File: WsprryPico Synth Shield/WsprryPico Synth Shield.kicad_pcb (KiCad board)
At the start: 2 copper layers, 53.3 x 22.9 mm, 1 part

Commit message: Set up schematic
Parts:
- U11: moved to B.Cu
- moved U11 1.95 mm to (146.8, 90.8), turned to -90 degrees
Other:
- outline, holes or cut-outs redrawn

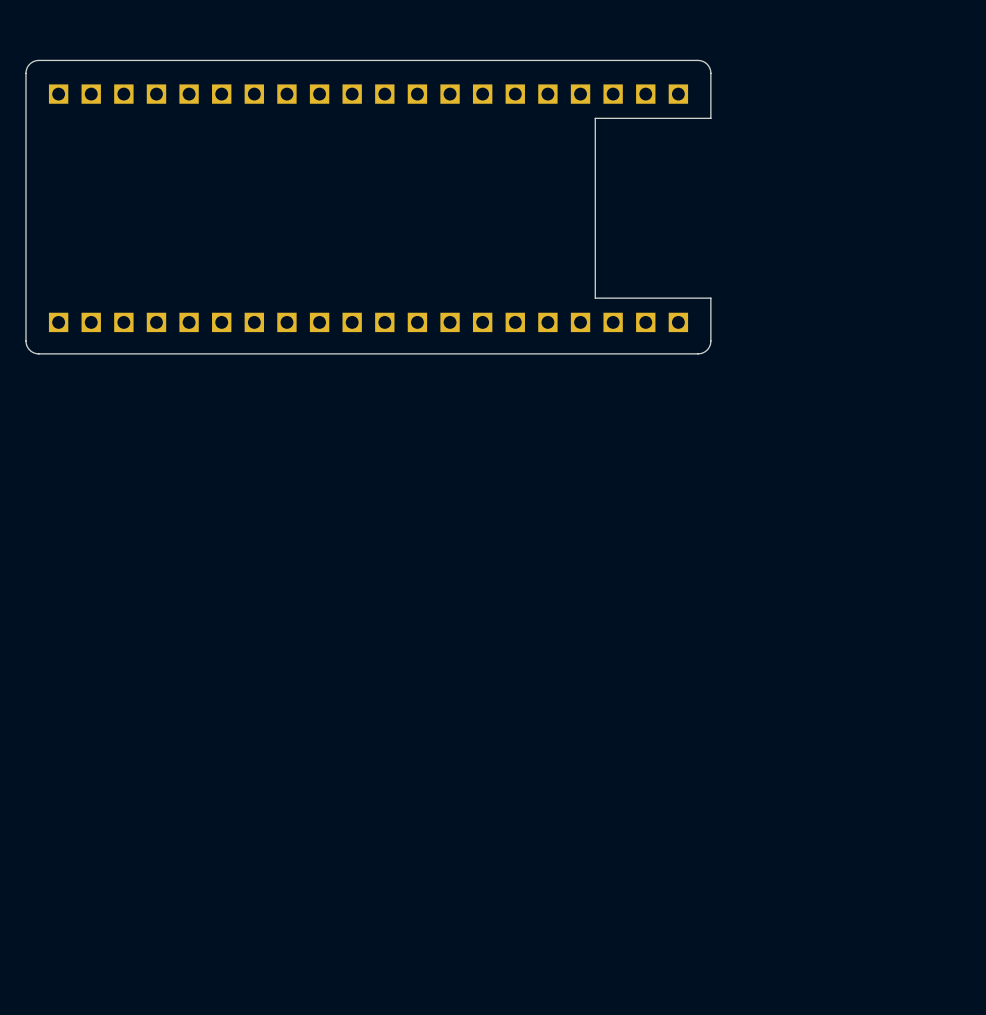
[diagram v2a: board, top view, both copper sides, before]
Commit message: Add single-post QLG3 variant and restore edge-launch SMA
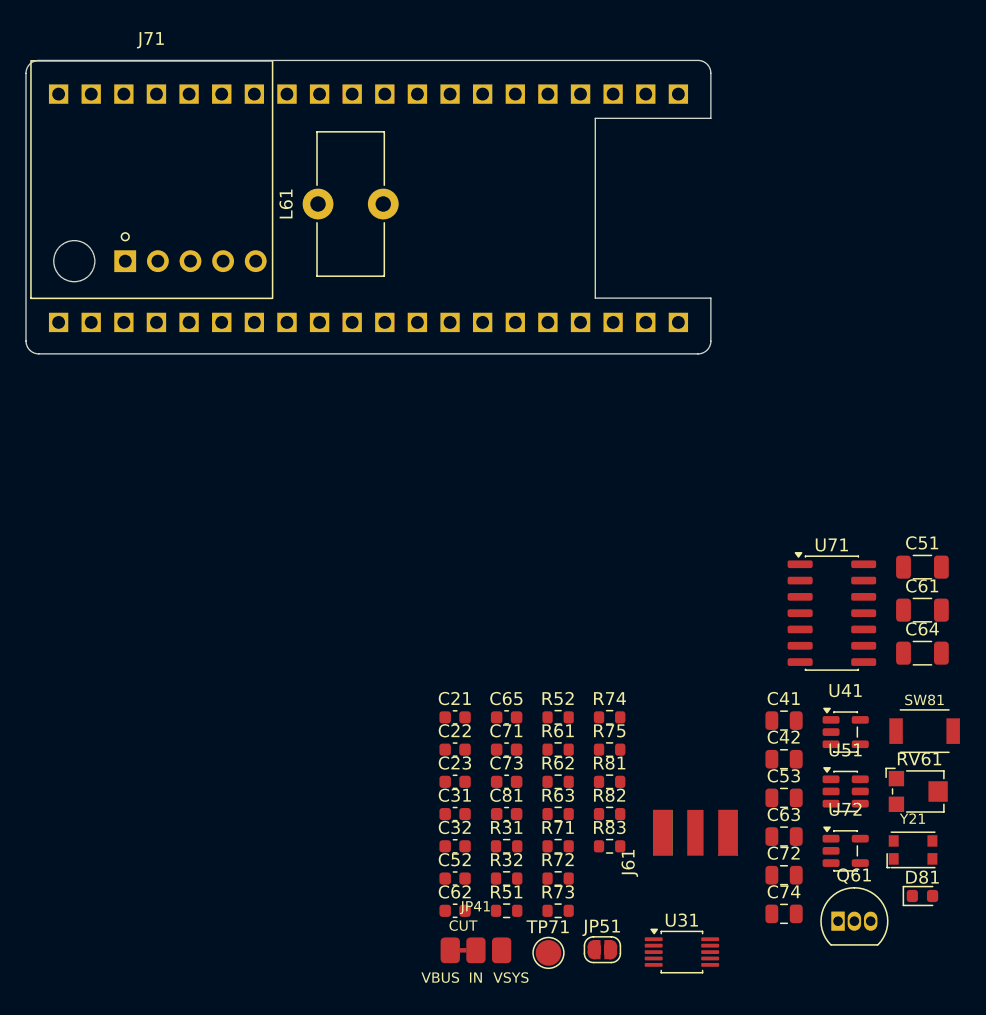
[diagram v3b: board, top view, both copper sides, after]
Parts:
- added C21: 10nF, wsprrypico-synth-shield:C_0603_1608Metric, F.Cu at (153.5, 129.5)
- added C22: 1nF C0G, wsprrypico-synth-shield:C_0603_1608Metric, F.Cu at (153.5, 132.0)
- added C23: 100nF, wsprrypico-synth-shield:C_0603_1608Metric, F.Cu at (153.5, 134.5)
- added C31: 100nF, wsprrypico-synth-shield:C_0603_1608Metric, F.Cu at (153.5, 137.0)
- added C32: 100nF, wsprrypico-synth-shield:C_0603_1608Metric, F.Cu at (153.5, 139.5)
- added C41: 2.2μF, wsprrypico-synth-shield:C_0805_2012Metric, F.Cu at (179.2, 129.8)
- added C42: 2.2μF, wsprrypico-synth-shield:C_0805_2012Metric, F.Cu at (179.2, 132.8)
- added C51: 10μF, wsprrypico-synth-shield:C_1206_3216Metric, F.Cu at (189.9, 117.8)
- added C52: 1nF, wsprrypico-synth-shield:C_0603_1608Metric, F.Cu at (153.5, 142.1)
- added C53: 1μF, wsprrypico-synth-shield:C_0805_2012Metric, F.Cu at (179.2, 135.8)
- added C61: 100nF, wsprrypico-synth-shield:C_1206_3216Metric, F.Cu at (189.9, 121.2)
- added C62: 100nF, wsprrypico-synth-shield:C_0603_1608Metric, F.Cu at (153.5, 144.6)
- added C63: 1μF, wsprrypico-synth-shield:C_0805_2012Metric, F.Cu at (179.2, 138.8)
- added C64: 100nF, wsprrypico-synth-shield:C_1206_3216Metric, F.Cu at (189.9, 124.5)
- added C65: 100nF, wsprrypico-synth-shield:C_0603_1608Metric, F.Cu at (157.6, 129.5)
- added C71: 100nF, wsprrypico-synth-shield:C_0603_1608Metric, F.Cu at (157.6, 132.0)
- added C72: 1μF, wsprrypico-synth-shield:C_0805_2012Metric, F.Cu at (179.2, 141.8)
- added C73: 100nF, wsprrypico-synth-shield:C_0603_1608Metric, F.Cu at (157.6, 134.5)
- added C74: 2.2μF, wsprrypico-synth-shield:C_0805_2012Metric, F.Cu at (179.2, 144.8)
- added C81: 10nF, wsprrypico-synth-shield:C_0603_1608Metric, F.Cu at (157.6, 137.0)
- added D81: Red, wsprrypico-synth-shield:LED_0603_1608Metric, F.Cu at (189.9, 143.4)
- added J61: SMA 50ohm, wsprrypico-synth-shield:SMA_Adafruit_1865_EdgeMount, F.Cu at (172.3, 140.8)
- added J71: QLG3 GPS Receiver, wsprrypico-synth-shield:QLG3_GPS_UndersideHeader_SinglePost, F.Cu at (120.7, 96.7)
- added JP41: SolderJumper_3_Bridged12, wsprrypico-synth-shield:PowerSelector_VBUS_IN_VSYS_Cuttable, F.Cu at (155.2, 147.6)
- added JP51: BIAS_SET, wsprrypico-synth-shield:SolderJumper-2_P1.3mm_Open_RoundedPad1.0x1.5mm, F.Cu at (165.0, 147.6)
- added L61: 25T FT37-43, wsprrypico-synth-shield:L_Toroid_FT37-43_Vertical_P5.08mm, F.Cu at (142.9, 89.5)
- added Q61: BS170, wsprrypico-synth-shield:TO-92_Inline, F.Cu at (183.4, 145.4)
- added R31: 4.7kΩ, wsprrypico-synth-shield:R_0603_1608Metric, F.Cu at (157.6, 139.5)
- added R32: 4.7kΩ, wsprrypico-synth-shield:R_0603_1608Metric, F.Cu at (157.6, 142.1)
- added R51: 100kΩ, wsprrypico-synth-shield:R_0603_1608Metric, F.Cu at (157.6, 144.6)
- added R52: 1kΩ, wsprrypico-synth-shield:R_0603_1608Metric, F.Cu at (161.6, 129.5)
- added R61: 22Ω, wsprrypico-synth-shield:R_0603_1608Metric, F.Cu at (161.6, 132.0)
- added R62: 4.7kΩ, wsprrypico-synth-shield:R_0603_1608Metric, F.Cu at (161.6, 134.5)
- added R63: 100kΩ, wsprrypico-synth-shield:R_0603_1608Metric, F.Cu at (161.6, 137.0)
- added R71: 10kΩ, wsprrypico-synth-shield:R_0603_1608Metric, F.Cu at (161.6, 139.5)
- added R72: 10kΩ, wsprrypico-synth-shield:R_0603_1608Metric, F.Cu at (161.6, 142.1)
- added R73: 100kΩ, wsprrypico-synth-shield:R_0603_1608Metric, F.Cu at (161.6, 144.6)
- added R74: 33Ω, wsprrypico-synth-shield:R_0603_1608Metric, F.Cu at (165.6, 129.5)
- added R75: 1kΩ, wsprrypico-synth-shield:R_0603_1608Metric, F.Cu at (165.6, 132.0)
- added R81: 10kΩ, wsprrypico-synth-shield:R_0603_1608Metric, F.Cu at (165.6, 134.5)
- added R82: 1kΩ, wsprrypico-synth-shield:R_0603_1608Metric, F.Cu at (165.6, 137.0)
- added R83: 1kΩ, wsprrypico-synth-shield:R_0603_1608Metric, F.Cu at (165.6, 139.5)
- added RV61: 5kΩ, wsprrypico-synth-shield:Potentiometer_Bourns_TC33X_Vertical, F.Cu at (189.7, 135.3)
- added SW81: Push, wsprrypico-synth-shield:SW_SPST_XUNPU_TS1088R_4x3mm, F.Cu at (190.1, 130.6)
- added TP71: GPS_RX, wsprrypico-synth-shield:TestPoint_Pad_D2.0mm, F.Cu at (160.8, 147.8)
- added U31: Si5351A-B-GTR, wsprrypico-synth-shield:MSOP-10_Si5351A_3x3mm_P0.5mm, F.Cu at (171.2, 147.8)
- added U41: TPS7A2033, wsprrypico-synth-shield:SOT-23-5, F.Cu at (184.0, 130.7)
- added U51: TPS22918, wsprrypico-synth-shield:SOT-23-6, F.Cu at (184.0, 135.3)
- added U71: LS7366R-S, wsprrypico-synth-shield:SOIC-14_3.9x8.7mm_P1.27mm, F.Cu at (182.9, 121.4)
- added U72: SN74LVC1G14, wsprrypico-synth-shield:SOT-23-5, F.Cu at (184.0, 139.9)
- added Y21: 25MHz TCXO, wsprrypico-synth-shield:KDS_DSB321SDN_3.2x2.5mm, F.Cu at (189.2, 139.8)
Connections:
- U11 pad 1: unconnected-(U11-GP0-Pad1) -> /GPS_RX
- U11 pad 13: unconnected-(U11-GND-Pad13) -> GND
- U11 pad 14: unconnected-(U11-GP10-Pad14) -> /COUNTER_SCK
- U11 pad 15: unconnected-(U11-GP11-Pad15) -> /COUNTER_MOSI
- U11 pad 16: unconnected-(U11-GP12-Pad16) -> /COUNTER_MISO
- U11 pad 17: unconnected-(U11-GP13-Pad17) -> /COUNTER_CS_N
- U11 pad 18: unconnected-(U11-GND-Pad18) -> GND
- U11 pad 19: unconnected-(U11-GP14-Pad19) -> /BUTTON_N
- U11 pad 2: unconnected-(U11-GP1-Pad2) -> /GPS_TX
- U11 pad 20: unconnected-(U11-GP15-Pad20) -> /LED_DRIVE
- U11 pad 21: unconnected-(U11-GP16-Pad21) -> /GPS_PPS
- U11 pad 22: unconnected-(U11-GP17-Pad22) -> /COUNTER_IRQ_N
- U11 pad 23: unconnected-(U11-GND-Pad23) -> GND
- U11 pad 28: unconnected-(U11-GND-Pad28) -> GND
- U11 pad 3: unconnected-(U11-GND-Pad3) -> GND
- U11 pad 33: unconnected-(U11-AGND-Pad33) -> GND
- U11 pad 36: unconnected-(U11-3V3_OUT-Pad36) -> /PICO_3V3
- U11 pad 38: unconnected-(U11-GND-Pad38) -> GND
- U11 pad 39: unconnected-(U11-VSYS-Pad39) -> /VSYS
- U11 pad 40: unconnected-(U11-VBUS-Pad40) -> /VBUS
- U11 pad 6: unconnected-(U11-GP4-Pad6) -> /SYNTH_SDA
- U11 pad 7: unconnected-(U11-GP5-Pad7) -> /SYNTH_SCL
- U11 pad 8: unconnected-(U11-GND-Pad8) -> GND
- U11 pad 9: unconnected-(U11-GP6-Pad9) -> /AMP_EN

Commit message: Save Synth layout progress and localize TP71 through-hole footprint
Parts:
- TP71: footprint wsprrypico-synth-shield:TestPoint_Pad_D2.0mm -> wsprrypico-synth-shield:TestPoint_THTPad_1.0x1.0mm_Drill0.5mm
- moved Q61 78.0 mm to (134.0, 85.0)
- moved TP71 75.4 mm to (122.7, 82.8)
- moved J61 73.9 mm to (121.3, 87.3), turned to -90 degrees
- moved C64 72.3 mm to (128.0, 87.3), turned to 180 degrees
- moved R63 60.3 mm to (131.1, 85.0), turned to 90 degrees
- moved R62 53.9 mm to (131.2, 90.0)
- moved R73 52.9 mm to (138.2, 97.0)
- moved R75 46.3 mm to (135.3, 97.0)
- moved L61 3.58 mm to (146.2, 88.3), turned to -90 degrees
- moved J71 0.57 mm to (120.6, 97.2)
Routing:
- net /GPS_PPS: track 0.00 -> 40.8 mm
- net /GPS_TX: track 0.00 -> 20.7 mm
- net /PICO_3V3: track 0.00 -> 7.78 mm
- net GND: track 0.00 -> 3.30 mm, vias 0 -> 3
- net /GPS_PPS_RAW: track 0.00 -> 3.15 mm
- net /TX_OUT: track 0.00 -> 2.96 mm
- net /GPS_RX: track 0.00 -> 1.78 mm
- added copper zone on B.Cu, net GND

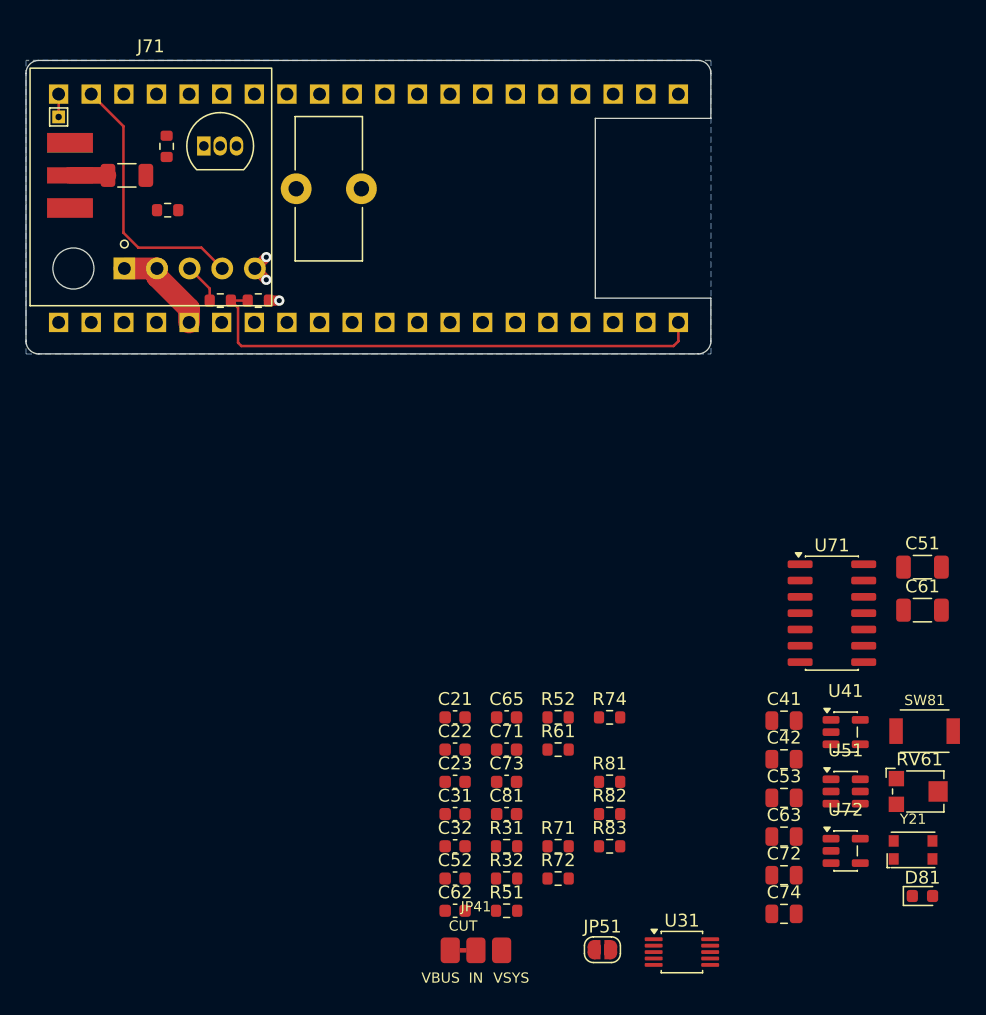
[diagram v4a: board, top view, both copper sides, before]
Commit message: Add onboard 90-series GPS receiver to Pico synth shield
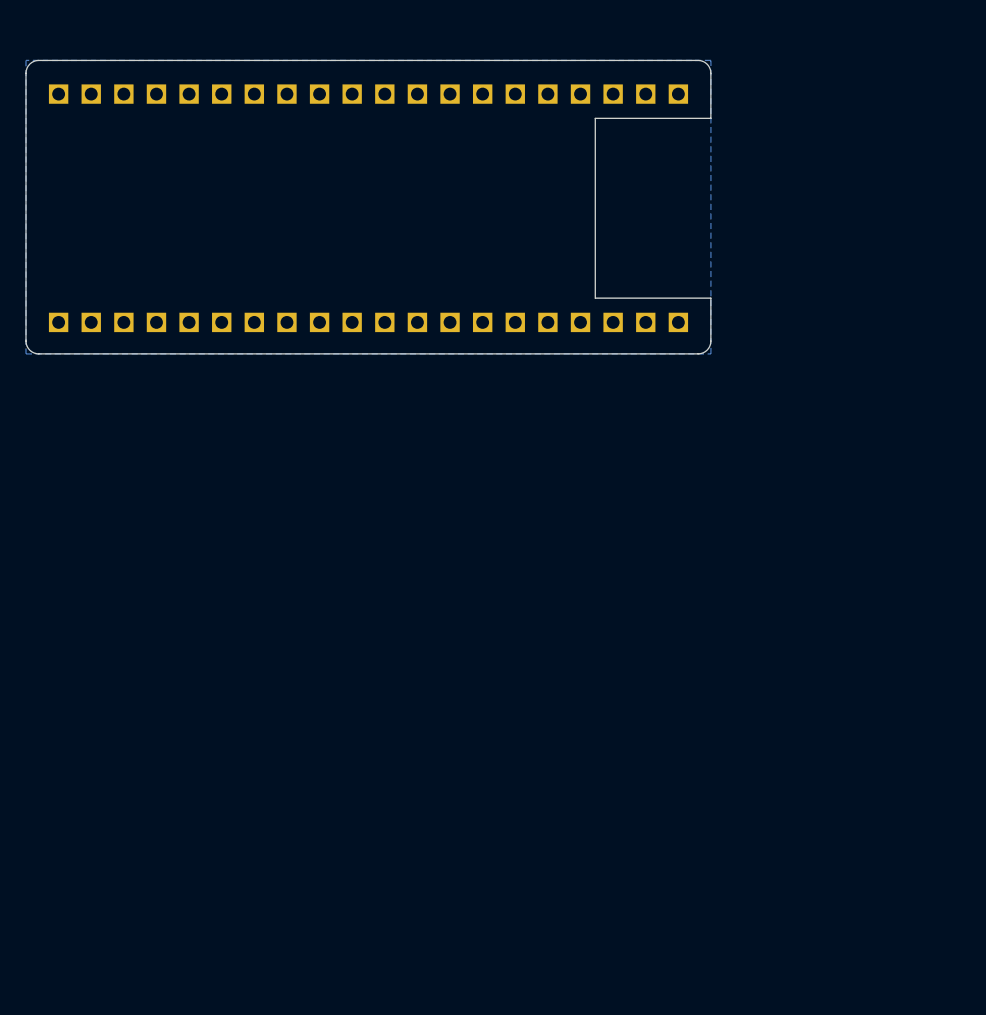
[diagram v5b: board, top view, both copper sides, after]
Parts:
- removed C21, C81: 10nF, wsprrypico-synth-shield:C_0603_1608Metric
- removed C22: 1nF C0G, wsprrypico-synth-shield:C_0603_1608Metric
- removed C23, C31, C32, C62, C65, C71, C73: 100nF, wsprrypico-synth-shield:C_0603_1608Metric
- removed C41, C42, C74: 2.2μF, wsprrypico-synth-shield:C_0805_2012Metric
- removed C51: 10μF, wsprrypico-synth-shield:C_1206_3216Metric
- removed C52: 1nF, wsprrypico-synth-shield:C_0603_1608Metric
- removed C53, C63, C72: 1μF, wsprrypico-synth-shield:C_0805_2012Metric
- removed C61, C64: 100nF, wsprrypico-synth-shield:C_1206_3216Metric
- removed D81: Red, wsprrypico-synth-shield:LED_0603_1608Metric
- removed J61: SMA 50ohm, wsprrypico-synth-shield:SMA_Adafruit_1865_EdgeMount
- removed J71: QLG3 GPS Receiver, wsprrypico-synth-shield:QLG3_GPS_UndersideHeader_SinglePost
- removed JP41: SolderJumper_3_Bridged12, wsprrypico-synth-shield:PowerSelector_VBUS_IN_VSYS_Cuttable
- removed JP51: BIAS_SET, wsprrypico-synth-shield:SolderJumper-2_P1.3mm_Open_RoundedPad1.0x1.5mm
- removed L61: 25T FT37-43, wsprrypico-synth-shield:L_Toroid_FT37-43_Vertical_P5.08mm
- removed Q61: BS170, wsprrypico-synth-shield:TO-92_Inline
- removed R31, R32, R62: 4.7kΩ, wsprrypico-synth-shield:R_0603_1608Metric
- removed R51, R63, R73: 100kΩ, wsprrypico-synth-shield:R_0603_1608Metric
- removed R52, R75, R82, R83: 1kΩ, wsprrypico-synth-shield:R_0603_1608Metric
- removed R61: 22Ω, wsprrypico-synth-shield:R_0603_1608Metric
- removed R71, R72, R81: 10kΩ, wsprrypico-synth-shield:R_0603_1608Metric
- removed R74: 33Ω, wsprrypico-synth-shield:R_0603_1608Metric
- removed RV61: 5kΩ, wsprrypico-synth-shield:Potentiometer_Bourns_TC33X_Vertical
- removed SW81: Push, wsprrypico-synth-shield:SW_SPST_XUNPU_TS1088R_4x3mm
- removed TP71: GPS_RX, wsprrypico-synth-shield:TestPoint_THTPad_1.0x1.0mm_Drill0.5mm
- removed U31: Si5351A-B-GTR, wsprrypico-synth-shield:MSOP-10_Si5351A_3x3mm_P0.5mm
- removed U41: TPS7A2033, wsprrypico-synth-shield:SOT-23-5
- removed U51: TPS22918, wsprrypico-synth-shield:SOT-23-6
- removed U71: LS7366R-S, wsprrypico-synth-shield:SOIC-14_3.9x8.7mm_P1.27mm
- removed U72: SN74LVC1G14, wsprrypico-synth-shield:SOT-23-5
- removed Y21: 25MHz TCXO, wsprrypico-synth-shield:KDS_DSB321SDN_3.2x2.5mm
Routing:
- net /GPS_PPS: track 40.8 -> 0.00 mm
- net /GPS_TX: track 20.7 -> 0.00 mm
- net /PICO_3V3: track 7.78 -> 0.00 mm
- net GND: track 3.30 -> 0.00 mm, vias 3 -> 0
- net /GPS_PPS_RAW: track 3.15 -> 0.00 mm
- net /TX_OUT: track 2.96 -> 0.00 mm
- net /GPS_RX: track 1.78 -> 0.00 mm
